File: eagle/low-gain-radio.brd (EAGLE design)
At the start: 99 x 100 mm, 119 parts, among them U1 MKW01Z128, U2 SKY65116, U3 W25Q80DV, U4 LP5907MFX-3.3, U5 NC7SZ05, U6 LP5907MFX-3.3, U7 LD39200, U8 MAAL-010704, U9 SKY13405-490LF, Y1 32MHz

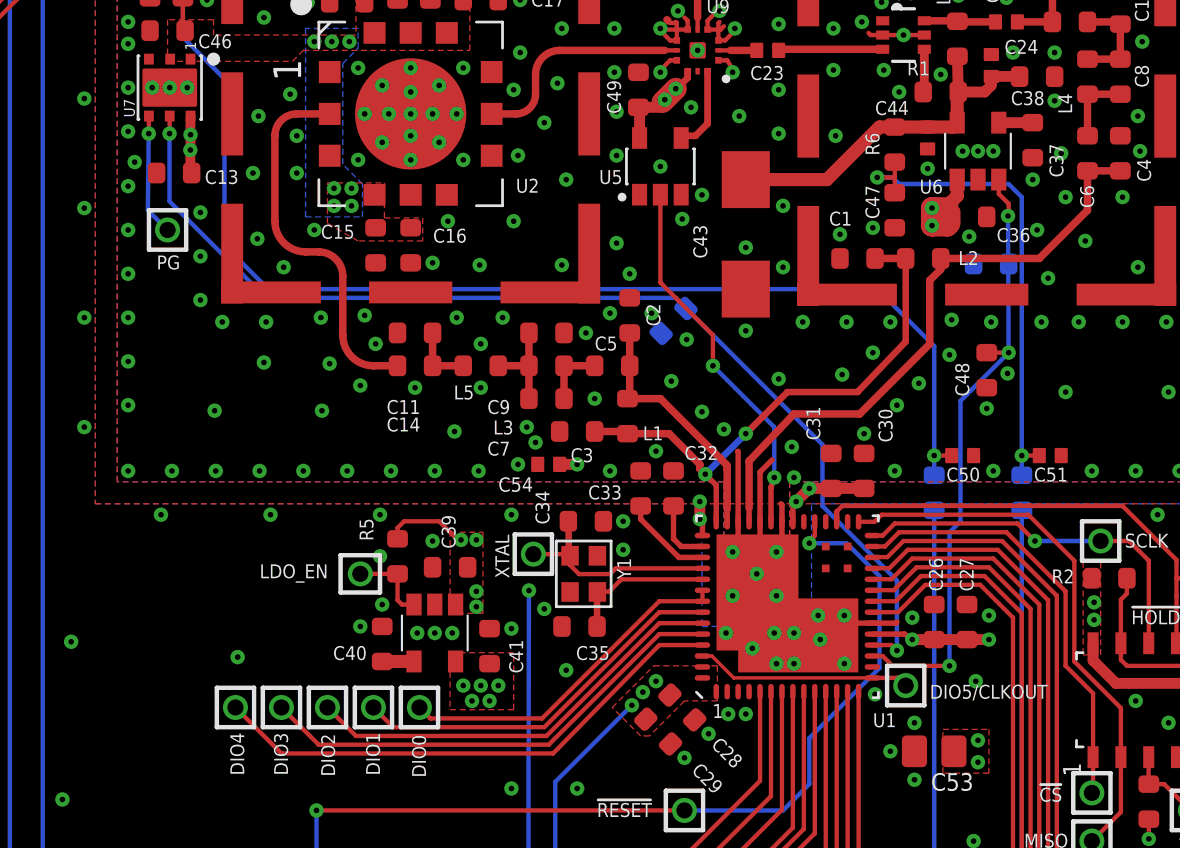
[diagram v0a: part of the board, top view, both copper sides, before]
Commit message: Added test points for LNA and PA EN lines
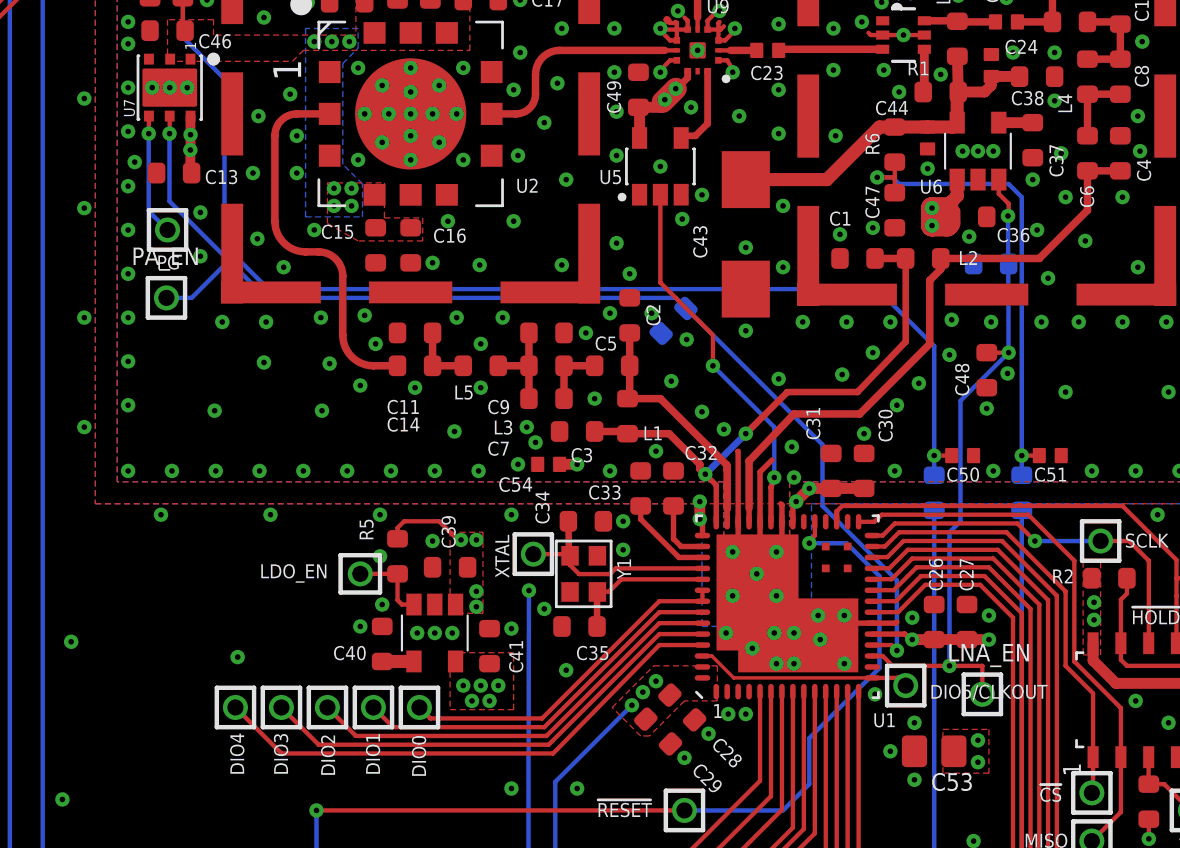
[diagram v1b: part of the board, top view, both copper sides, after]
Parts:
- added LNA_EN, PA_EN: TEST-POINT, Tova:2MM-TEST-POINT
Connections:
- net LNA_EN: now also LNA_EN.1
- net PA_EN: now also PA_EN.1
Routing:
- net PA_EN: track 50.4 -> 54.0 mm
- net LNA_EN: track 28.3 -> 31.1 mm
- net RF_GND: vias 285 -> 284
- net GND: vias 181 -> 180
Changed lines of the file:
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@@
 <grid distance="0.05" unitdist="mm" unit="mm" style="lines" multiple="1" display="yes" altdistance="0.025" altunitdist="inch" altunit="inch"/>
 <layers>
-<layer number="1" name="Top" color="4" fill="1" visible="no" active="yes"/>
+<layer number="1" name="Top" color="4" fill="1" visible="yes" active="yes"/>
 <layer number="2" name="Route2" color="15" fill="1" visible="no" active="yes"/>
 <layer number="3" name="Route3" color="4" fill="3" visible="no" active="no"/>
@@
 <attribute name="DPN" value="311-10.0KHRCT-ND" x="85.4" y="73.95" size="1.778" layer="28" rot="MR0" display="off"/>
 </element>
+<element name="PA_EN" library="Tova" package="2MM-TEST-POINT" value="TEST-POINT" x="47.75" y="72.4"/>
+<element name="LNA_EN" library="Tova" package="2MM-TEST-POINT" value="TEST-POINT" x="85" y="54.3"/>
 </elements>
 <signals>
@@
 <via x="81.9" y="53" extent="1-16" drill="0.254" diameter="0.245"/>
 <via x="81.9" y="50.4" extent="1-16" drill="0.254" diameter="0.245"/>
-<via x="84.7" y="54.9" extent="1-16" drill="0.254" diameter="0.245"/>
+<wire x1="84.7" y1="54.9" x2="84.7" y2="54.9" width="0" layer="19" extent="1-16"/>
 <via x="78.7" y="57.9" extent="1-16" drill="0.254"/>
 <via x="78.7" y="55.7" extent="1-16" drill="0.254"/>
@@
 <wire x1="47.9" y1="80.7" x2="47.8908125" y2="79.9" width="0.2" layer="1"/>
 <wire x1="47.8908125" y1="79.9" x2="47.8908125" y2="76.8091875" width="0.2" layer="16"/>
-<wire x1="47.8908125" y1="76.8091875" x2="52.3" y2="72.4" width="0.2" layer="16"/>
+<wire x1="47.8908125" y1="76.8091875" x2="50.6" y2="74.1" width="0.2" layer="16"/>
+<wire x1="50.6" y1="74.1" x2="52.3" y2="72.4" width="0.2" layer="16"/>
 <wire x1="52.3" y1="72.4" x2="71" y2="72.4" width="0.2" layer="16"/>
 <wire x1="79.9778" y1="56.55" x2="80.85" y2="56.55" width="0.2" layer="1"/>
@@
 <wire x1="71.4656875" y1="71.915684375" x2="71.525" y2="71.915684375" width="0.4064" layer="16"/>
 <wire x1="71.525" y1="71.915684375" x2="71.525" y2="71.875" width="0.4064" layer="16"/>
+<contactref element="PA_EN" pad="1"/>
+<wire x1="47.75" y1="72.4" x2="48.9" y2="72.4" width="0.2" layer="16"/>
+<wire x1="48.9" y1="72.4" x2="50.6" y2="74.1" width="0.2" layer="16"/>
 </signal>
 <signal name="LNA_EN">
@@
 <wire x1="86.2" y1="73.95" x2="86.1802875" y2="73.95" width="0.4064" layer="16"/>
 <wire x1="86.1802875" y1="73.95" x2="86.1802875" y2="73.99990625" width="0.4064" layer="16"/>
+<contactref element="LNA_EN" pad="1"/>
+<wire x1="85" y1="54.3" x2="85" y2="55.6" width="0.2" layer="1"/>
+<wire x1="85" y1="55.6" x2="83.5" y2="55.6" width="0.2" layer="1"/>
 </signal>
 <signal name="N$43" class="1">
@@
 <wire x1="46.95" y1="80.7" x2="46.9408125" y2="79.9" width="0.2" layer="1"/>
 <via x="46.9408125" y="79.9" extent="1-16" drill="0.254"/>
-<wire x1="46.9408125" y1="79.9" x2="46.9" y2="76.4" width="0.2" layer="16"/>
-<wire x1="46.9" y1="76.4" x2="47.8" y2="75.5" width="0.2" layer="16"/>
+<wire x1="46.9408125" y1="79.9" x2="46.9408125" y2="76.3591875" width="0.2" layer="16"/>
+<wire x1="46.9408125" y1="76.3591875" x2="47.8" y2="75.5" width="0.2" layer="16"/>
 </signal>
 <signal name="!HOLD">
@@
 <via x="93.4" y="71.3" extent="1-16" drill="0.254" diameter="0.245"/>
 <via x="49.3" y="76.3" extent="1-16" drill="0.254" diameter="0.245"/>
-<via x="49.3" y="72.3" extent="1-16" drill="0.254" diameter="0.245"/>
+<wire x1="49.3" y1="72.3" x2="49.3" y2="72.3" width="0" layer="19" extent="1-16"/>
 <via x="49.3" y="74.3" extent="1-16" drill="0.254" diameter="0.245"/>
 <via x="54.8" y="71.5" extent="1-16" drill="0.254" diameter="0.245"/>

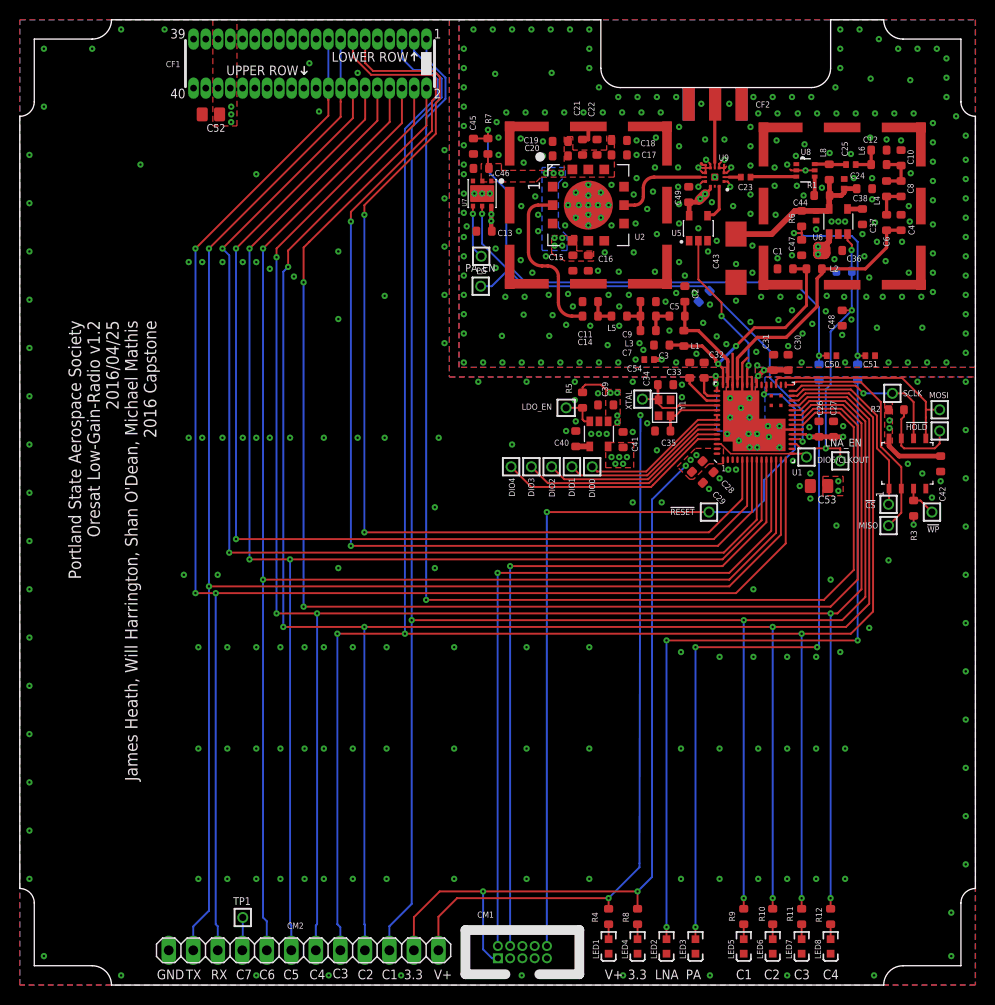
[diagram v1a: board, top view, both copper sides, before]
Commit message: Added LEDs for Rx and Tx
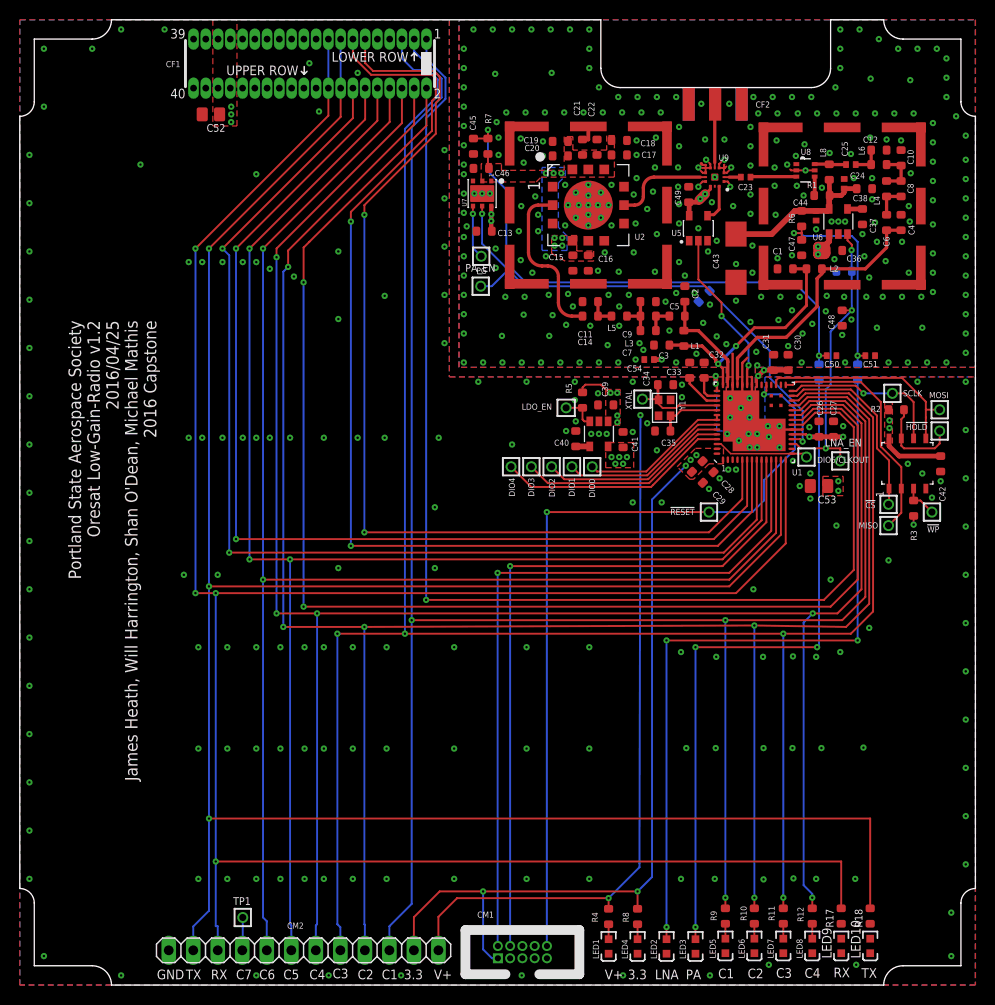
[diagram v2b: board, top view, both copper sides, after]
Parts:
- added LED10, LED9: DNP/GRN, psas_c3_team05:LED-0603
- added R17, R18: DNP/1k, rcl_custom:.0603-B-NOSILK@1
- moved LED5 1.90 mm to (73.1, 4.05)
- moved LED6 1.90 mm to (76.1, 4.05)
- moved LED7 1.90 mm to (79.1, 4.05)
- moved LED8 1.90 mm to (82.1, 4.05)
- moved R10 1.90 mm to (76.1, 7.15)
- moved R11 1.90 mm to (79.1, 7.15)
- moved R12 1.90 mm to (82.1, 7.15)
- moved R9 1.90 mm to (73.1, 7.15)
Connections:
- new net N$6: LED9.A, R17.1
- new net N$9: LED10.A, R18.1
- net GND: now also LED10.K, LED9.K
- net UART0_RX: now also R17.2
- net UART0_TX: now also R18.2
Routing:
- net UART0_TX: track 170.0 -> 247.8 mm, vias 2 -> 3
- net UART0_RX: track 172.1 -> 241.9 mm, vias 3 -> 4
- net PTC4: track 212.6 -> 213.4 mm

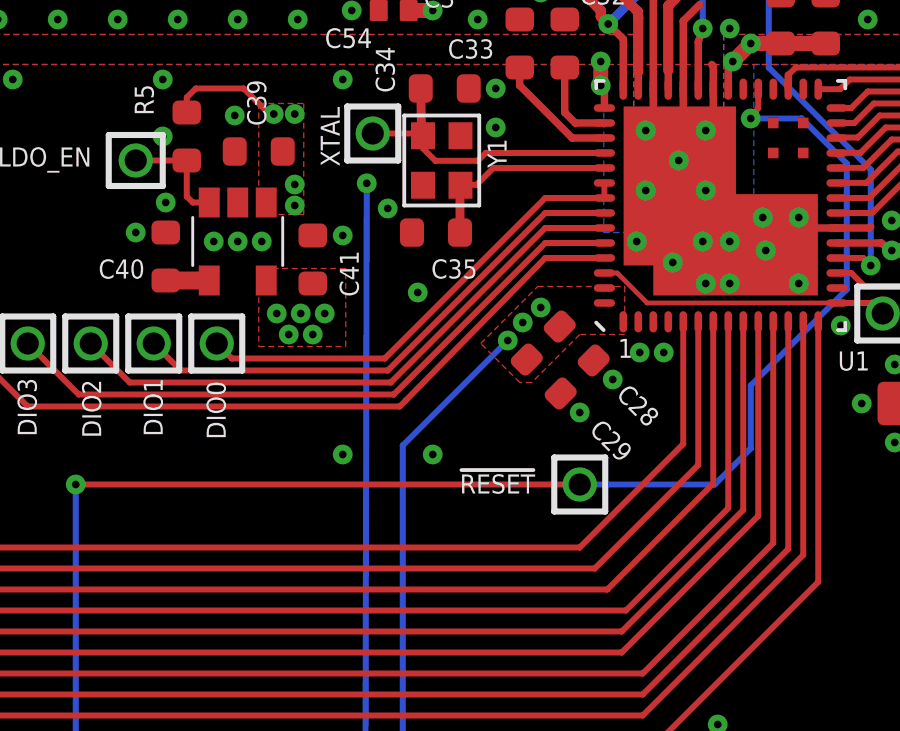
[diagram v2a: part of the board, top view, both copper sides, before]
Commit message: Attached RESET(RF) to PTE16 instead of having it attached to DIO0
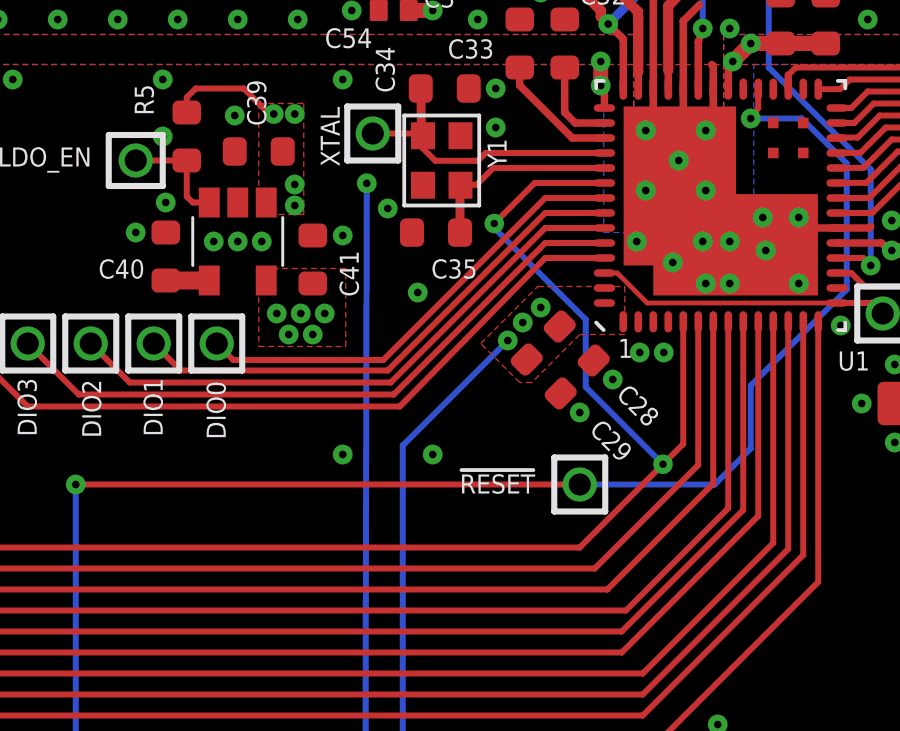
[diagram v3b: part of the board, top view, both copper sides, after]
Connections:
- removed net DIO0: DIO0.1, U1.48, U1.49
- new net N$11: DIO0.1, U1.49
- net PTE16: now also U1.48
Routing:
- net DIO0: track 15.8 -> 0.00 mm
- net N$11: track 0.00 -> 15.4 mm
- net PTE16: track 105.9 -> 120.5 mm, vias 2 -> 4
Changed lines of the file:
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@@
 <layer number="23" name="tOrigins" color="15" fill="1" visible="yes" active="yes"/>
 <layer number="24" name="bOrigins" color="15" fill="1" visible="yes" active="yes"/>
-<layer number="25" name="tNames" color="7" fill="1" visible="no" active="yes"/>
+<layer number="25" name="tNames" color="7" fill="1" visible="yes" active="yes"/>
 <layer number="26" name="bNames" color="7" fill="1" visible="no" active="yes"/>
 <layer number="27" name="tValues" color="7" fill="1" visible="no" active="yes"/>
@@
 <wire x1="43.1" y1="88.2" x2="35.7" y2="80.8" width="0.2" layer="1"/>
 <via x="35.7" y="79.8" extent="1-16" drill="0.254"/>
-<wire x1="74.85" y1="50.35" x2="71.4" y2="46.9" width="0.2" layer="1"/>
+<wire x1="74.85" y1="50.35" x2="74.175" y2="49.675" width="0.2" layer="1"/>
+<wire x1="74.175" y1="49.675" x2="71.4" y2="46.9" width="0.2" layer="1"/>
 <wire x1="35.7" y1="79.8" x2="35.7" y2="80.8" width="0.2" layer="1"/>
+<contactref element="U1" pad="48"/>
+<wire x1="72.2222" y1="59.05" x2="69.9" y2="59.05" width="0.2" layer="1"/>
+<wire x1="69.9" y1="59.05" x2="68.55" y2="57.7" width="0.2" layer="1"/>
+<via x="68.55" y="57.7" extent="1-16" drill="0.245"/>
+<wire x1="68.55" y1="57.7" x2="68.55" y2="57.55" width="0.2" layer="16"/>
+<wire x1="68.55" y1="57.55" x2="71.6" y2="54.5" width="0.2" layer="16"/>
+<wire x1="71.6" y1="54.5" x2="71.6" y2="52.25" width="0.2" layer="16"/>
+<wire x1="71.6" y1="52.25" x2="74.175" y2="49.675" width="0.2" layer="16"/>
+<via x="74.175" y="49.675" extent="1-16" drill="0.245"/>
 </signal>
 <signal name="PTE17">
@@
 <wire x1="53" y1="51.6" x2="50.9" y2="53.7" width="0.2" layer="1"/>
 </signal>
-<signal name="DIO0">
-<contactref element="U1" pad="49"/>
-<contactref element="U1" pad="48"/>
-<wire x1="72.2222" y1="59.05" x2="72.2222" y2="58.55" width="0.2" layer="1"/>
-<contactref element="DIO0" pad="1"/>
-<wire x1="72.2222" y1="58.55" x2="70.25" y2="58.55" width="0.2" layer="1"/>
-<wire x1="70.25" y1="58.55" x2="64.9" y2="53.2" width="0.2" layer="1"/>
-<wire x1="64.9" y1="53.2" x2="59.8" y2="53.2" width="0.2" layer="1"/>
-<wire x1="59.8" y1="53.2" x2="59.3" y2="53.7" width="0.2" layer="1"/>
-</signal>
 <signal name="DIO1">
 <contactref element="U1" pad="50"/>
@@
 <wire x1="88.1" y1="4.8" x2="88.1" y2="6.35" width="0" layer="19" extent="1-1"/>
 </signal>
+<signal name="N$11">
+<contactref element="U1" pad="49"/>
+<contactref element="DIO0" pad="1"/>
+<wire x1="59.3" y1="53.7" x2="59.85" y2="53.15" width="0.2" layer="1"/>
+<wire x1="59.85" y1="53.15" x2="64.85" y2="53.15" width="0.2" layer="1"/>
+<wire x1="64.85" y1="53.15" x2="70.25" y2="58.55" width="0.2" layer="1"/>
+<wire x1="70.25" y1="58.55" x2="72.2222" y2="58.55" width="0.2" layer="1"/>
+</signal>
 </signals>
